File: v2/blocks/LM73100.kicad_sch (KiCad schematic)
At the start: 13 parts, among them U5 LM73100RPWR

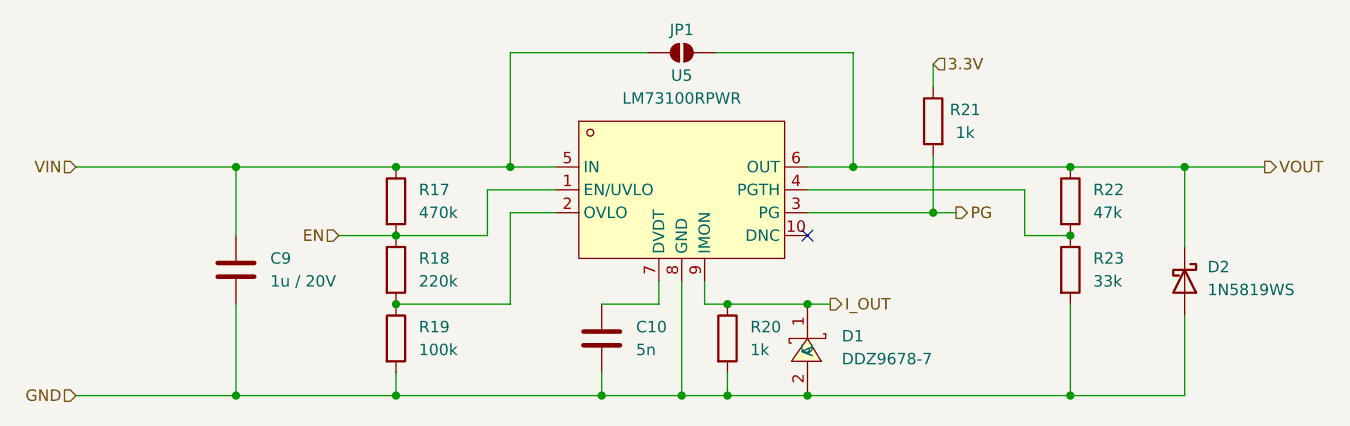
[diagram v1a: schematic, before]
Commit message: can transceiver and battery reverse polarity bypass
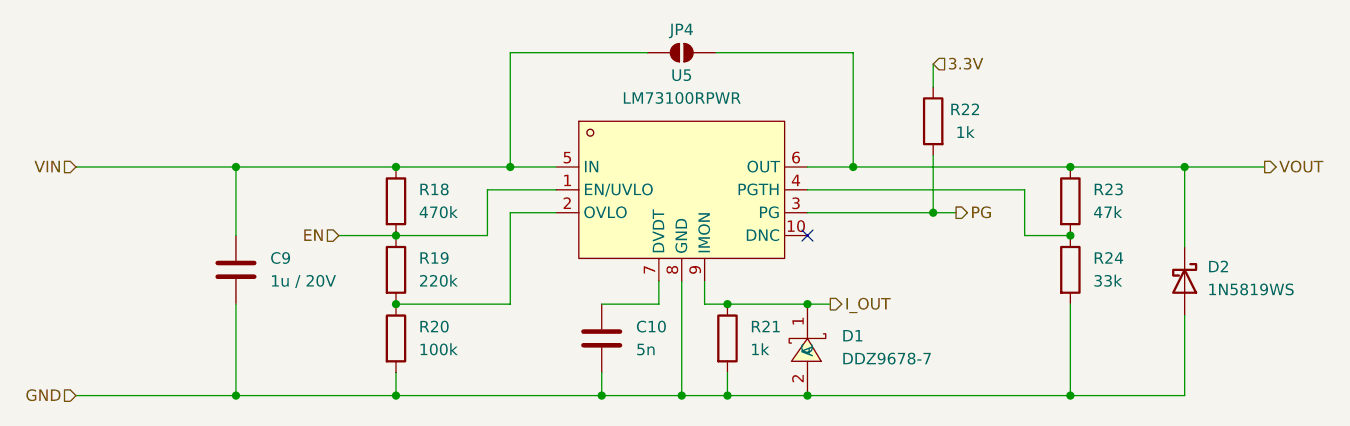
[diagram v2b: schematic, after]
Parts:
- renumbered JP1 to JP4, R17 to R18, R18 to R19, R19 to R20, R20 to R21, R21 to R22, R22 to R23, R23 to R24
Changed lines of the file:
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@@
 		(shape input)
 		(at 49.53 39.37 180)
+		(fields_autoplaced yes)
 		(effects
 			(font
@@
 		(shape output)
 		(at 133.35 54.61 0)
+		(fields_autoplaced yes)
 		(effects
 			(font
@@
 		(shape output)
 		(at 147.32 44.45 0)
+		(fields_autoplaced yes)
 		(effects
 			(font
@@
 		(shape input)
 		(at 144.78 27.94 0)
+		(fields_autoplaced yes)
 		(effects
 			(font
@@
 		(shape output)
 		(at 181.61 39.37 0)
+		(fields_autoplaced yes)
 		(effects
 			(font
@@
 		(shape input)
 		(at 78.74 46.99 180)
+		(fields_autoplaced yes)
 		(effects
 			(font
@@
 		(shape input)
 		(at 49.53 64.77 180)
+		(fields_autoplaced yes)
 		(effects
 			(font
@@
 		(dnp no)
 		(fields_autoplaced yes)
-		(property "Reference" "R23"
+		(property "Reference" "R24"
 			(at 162.56 49.5299 0)
 			(effects
@@
 			(project "EPSv2"
 				(path "/61d36b12-c329-4dd2-b08b-b63678fc7b25/94222426-b8c4-4788-b7e1-6bd67c2c6f83"
-					(reference "R23")
-					(unit 1)
-				)
-				(path "/61d36b12-c329-4dd2-b08b-b63678fc7b25/a7a8fd8d-cf1d-49ef-967f-092d6a685c3c"
-					(reference "R45")
-					(unit 1)
-				)
-				(path "/61d36b12-c329-4dd2-b08b-b63678fc7b25/dee2a6ed-6868-4094-81ad-adecb8e2dcf2"
-					(reference "R52")
+					(reference "R24")
+					(unit 1)
+				)
+				(path "/61d36b12-c329-4dd2-b08b-b63678fc7b25/a7a8fd8d-cf1d-49ef-967f-092d6a685c3c"
+					(reference "R46")
+					(unit 1)
+				)
+				(path "/61d36b12-c329-4dd2-b08b-b63678fc7b25/dee2a6ed-6868-4094-81ad-adecb8e2dcf2"
+					(reference "R53")
 					(unit 1)
 				)
@@
 		(on_board yes)
 		(dnp no)
-		(property "Reference" "JP1"
+		(property "Reference" "JP4"
 			(at 116.84 24.13 0)
 			(effects
@@
 			(project "EPSv2"
 				(path "/61d36b12-c329-4dd2-b08b-b63678fc7b25/94222426-b8c4-4788-b7e1-6bd67c2c6f83"
-					(reference "JP1")
-					(unit 1)
-				)
-				(path "/61d36b12-c329-4dd2-b08b-b63678fc7b25/a7a8fd8d-cf1d-49ef-967f-092d6a685c3c"
-					(reference "JP2")
-					(unit 1)
-				)
-				(path "/61d36b12-c329-4dd2-b08b-b63678fc7b25/dee2a6ed-6868-4094-81ad-adecb8e2dcf2"
-					(reference "JP3")
+					(reference "JP4")
+					(unit 1)
+				)
+				(path "/61d36b12-c329-4dd2-b08b-b63678fc7b25/a7a8fd8d-cf1d-49ef-967f-092d6a685c3c"
+					(reference "JP5")
+					(unit 1)
+				)
+				(path "/61d36b12-c329-4dd2-b08b-b63678fc7b25/dee2a6ed-6868-4094-81ad-adecb8e2dcf2"
+					(reference "JP6")
 					(unit 1)
 				)
@@
 		(dnp no)
 		(fields_autoplaced yes)
-		(property "Reference" "R17"
+		(property "Reference" "R18"
 			(at 87.63 41.9099 0)
 			(effects
@@
 			(project "EPSv2"
 				(path "/61d36b12-c329-4dd2-b08b-b63678fc7b25/94222426-b8c4-4788-b7e1-6bd67c2c6f83"
-					(reference "R17")
-					(unit 1)
-				)
-				(path "/61d36b12-c329-4dd2-b08b-b63678fc7b25/a7a8fd8d-cf1d-49ef-967f-092d6a685c3c"
-					(reference "R39")
-					(unit 1)
-				)
-				(path "/61d36b12-c329-4dd2-b08b-b63678fc7b25/dee2a6ed-6868-4094-81ad-adecb8e2dcf2"
-					(reference "R46")
+					(reference "R18")
+					(unit 1)
+				)
+				(path "/61d36b12-c329-4dd2-b08b-b63678fc7b25/a7a8fd8d-cf1d-49ef-967f-092d6a685c3c"
+					(reference "R40")
+					(unit 1)
+				)
+				(path "/61d36b12-c329-4dd2-b08b-b63678fc7b25/dee2a6ed-6868-4094-81ad-adecb8e2dcf2"
+					(reference "R47")
 					(unit 1)
 				)
@@
 		(dnp no)
 		(fields_autoplaced yes)
-		(property "Reference" "R22"
+		(property "Reference" "R23"
 			(at 162.56 41.91 0)
 			(effects
@@
 			(project "EPSv2"
 				(path "/61d36b12-c329-4dd2-b08b-b63678fc7b25/94222426-b8c4-4788-b7e1-6bd67c2c6f83"
-					(reference "R22")
-					(unit 1)
-				)
-				(path "/61d36b12-c329-4dd2-b08b-b63678fc7b25/a7a8fd8d-cf1d-49ef-967f-092d6a685c3c"
-					(reference "R44")
-					(unit 1)
-				)
-				(path "/61d36b12-c329-4dd2-b08b-b63678fc7b25/dee2a6ed-6868-4094-81ad-adecb8e2dcf2"
-					(reference "R51")
+					(reference "R23")
+					(unit 1)
+				)
+				(path "/61d36b12-c329-4dd2-b08b-b63678fc7b25/a7a8fd8d-cf1d-49ef-967f-092d6a685c3c"
+					(reference "R45")
+					(unit 1)
+				)
+				(path "/61d36b12-c329-4dd2-b08b-b63678fc7b25/dee2a6ed-6868-4094-81ad-adecb8e2dcf2"
+					(reference "R52")
 					(unit 1)
 				)
@@
 		(dnp no)
 		(fields_autoplaced yes)
-		(property "Reference" "R18"
+		(property "Reference" "R19"
 			(at 87.63 49.5299 0)
 			(effects
@@
 			(project "EPSv2"
 				(path "/61d36b12-c329-4dd2-b08b-b63678fc7b25/94222426-b8c4-4788-b7e1-6bd67c2c6f83"
-					(reference "R18")
-					(unit 1)
-				)
-				(path "/61d36b12-c329-4dd2-b08b-b63678fc7b25/a7a8fd8d-cf1d-49ef-967f-092d6a685c3c"
-					(reference "R40")
-					(unit 1)
-				)
-				(path "/61d36b12-c329-4dd2-b08b-b63678fc7b25/dee2a6ed-6868-4094-81ad-adecb8e2dcf2"
-					(reference "R47")
+					(reference "R19")
+					(unit 1)
+				)
+				(path "/61d36b12-c329-4dd2-b08b-b63678fc7b25/a7a8fd8d-cf1d-49ef-967f-092d6a685c3c"
+					(reference "R41")
+					(unit 1)
+				)
+				(path "/61d36b12-c329-4dd2-b08b-b63678fc7b25/dee2a6ed-6868-4094-81ad-adecb8e2dcf2"
+					(reference "R48")
 					(unit 1)
 				)
@@
 		(dnp no)
 		(fields_autoplaced yes)
-		(property "Reference" "R19"
+		(property "Reference" "R20"
 			(at 87.63 57.1499 0)
 			(effects
@@
 			(project "EPSv2"
 				(path "/61d36b12-c329-4dd2-b08b-b63678fc7b25/94222426-b8c4-4788-b7e1-6bd67c2c6f83"
-					(reference "R19")
-					(unit 1)
-				)
-				(path "/61d36b12-c329-4dd2-b08b-b63678fc7b25/a7a8fd8d-cf1d-49ef-967f-092d6a685c3c"
-					(reference "R41")
-					(unit 1)
-				)
-				(path "/61d36b12-c329-4dd2-b08b-b63678fc7b25/dee2a6ed-6868-4094-81ad-adecb8e2dcf2"
-					(reference "R48")
+					(reference "R20")
+					(unit 1)
+				)
+				(path "/61d36b12-c329-4dd2-b08b-b63678fc7b25/a7a8fd8d-cf1d-49ef-967f-092d6a685c3c"
+					(reference "R42")
+					(unit 1)
+				)
+				(path "/61d36b12-c329-4dd2-b08b-b63678fc7b25/dee2a6ed-6868-4094-81ad-adecb8e2dcf2"
+					(reference "R49")
 					(unit 1)
 				)
@@
 		(dnp no)
 		(fields_autoplaced yes)
-		(property "Reference" "R20"
+		(property "Reference" "R21"
 			(at 124.46 57.1499 0)
 			(effects
@@
 			(project "EPSv2"
 				(path "/61d36b12-c329-4dd2-b08b-b63678fc7b25/94222426-b8c4-4788-b7e1-6bd67c2c6f83"
-					(reference "R20")
-					(unit 1)
-				)
-				(path "/61d36b12-c329-4dd2-b08b-b63678fc7b25/a7a8fd8d-cf1d-49ef-967f-092d6a685c3c"
-					(reference "R42")
-					(unit 1)
-				)
-				(path "/61d36b12-c329-4dd2-b08b-b63678fc7b25/dee2a6ed-6868-4094-81ad-adecb8e2dcf2"
-					(reference "R49")
+					(reference "R21")
+					(unit 1)
+				)
+				(path "/61d36b12-c329-4dd2-b08b-b63678fc7b25/a7a8fd8d-cf1d-49ef-967f-092d6a685c3c"
+					(reference "R43")
+					(unit 1)
+				)
+				(path "/61d36b12-c329-4dd2-b08b-b63678fc7b25/dee2a6ed-6868-4094-81ad-adecb8e2dcf2"
+					(reference "R50")
 					(unit 1)
 				)
@@
 		(on_board yes)
 		(dnp no)
-		(property "Reference" "R21"
+		(property "Reference" "R22"
 			(at 148.336 33.02 0)
 			(effects
@@
 			(project "EPSv2"
 				(path "/61d36b12-c329-4dd2-b08b-b63678fc7b25/94222426-b8c4-4788-b7e1-6bd67c2c6f83"
-					(reference "R21")
-					(unit 1)
-				)
-				(path "/61d36b12-c329-4dd2-b08b-b63678fc7b25/a7a8fd8d-cf1d-49ef-967f-092d6a685c3c"
-					(reference "R43")
-					(unit 1)
-				)
-				(path "/61d36b12-c329-4dd2-b08b-b63678fc7b25/dee2a6ed-6868-4094-81ad-adecb8e2dcf2"
-					(reference "R50")
-					(unit 1)
-				)
+					(reference "R22")
+					(unit 1)
+				)
+				(path "/61d36b12-c329-4dd2-b08b-b63678fc7b25/a7a8fd8d-cf1d-49ef-967f-092d6a685c3c"
+					(reference "R44")
+					(unit 1)
+				)
+				(path "/61d36b12-c329-4dd2-b08b-b63678fc7b25/dee2a6ed-6868-4094-81ad-adecb8e2dcf2"
+					(reference "R51")
+					(unit 1)
+				)

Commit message: load switch default OFF
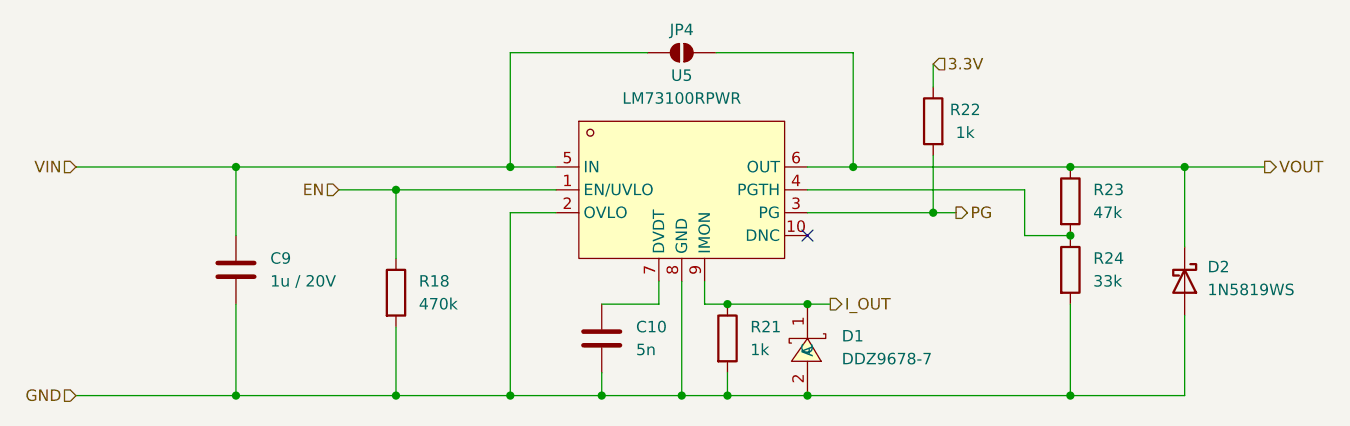
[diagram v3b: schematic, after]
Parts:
- removed R19: 220k, Resistor_SMD:R_0402_1005Metric, symbol Device:R
- removed R20: 100k, Resistor_SMD:R_0402_1005Metric, symbol Device:R
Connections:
- net EN: now also R18.1; no longer R18.2
- net GND: now also R18.2, U5.2 (OVLO)
- net VIN: no longer R18.1
